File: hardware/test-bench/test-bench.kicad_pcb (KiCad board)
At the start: 2 copper layers, 90 x 90 mm, 35 parts, among them J1 Conn_Mem_Ext, J2 Conn_Reg, J3 SWD, J4 Conn_Mem, J5 FTDI, J6 Conn_Power, SW1 SW_Push_4pin, SW2 SW_Push_4pin, U1 STM32G030F6, U2 MCP23S17_SS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

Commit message: Added test points
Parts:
- added TP1: TestPoint, TestPoint:TestPoint_THTPad_D2.0mm_Drill1.0mm, F.Cu at (135.6, 51.6)
- added TP2: TestPoint, TestPoint:TestPoint_THTPad_D2.0mm_Drill1.0mm, F.Cu at (180.8, 46.8)
- added TP3: TestPoint, TestPoint:TestPoint_THTPad_D2.0mm_Drill1.0mm, F.Cu at (189.8, 75.6)
- added TP4: TestPoint, TestPoint:TestPoint_THTPad_D2.0mm_Drill1.0mm, F.Cu at (133.4, 91.4)
- added TP5: TestPoint, TestPoint:TestPoint_Pad_2.0x2.0mm, F.Cu at (189.8, 80.7)
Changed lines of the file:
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@@
     (tracks 1000)
     (zones 0)
-    (modules 35)
+    (modules 40)
     (nets 118)
   )
@@
     (mod_text_size 1 1)
     (mod_text_width 0.15)
-    (pad_size 1.75 0.45)
+    (pad_size 2 2)
     (pad_drill 0)
     (pad_to_mask_clearance 0.051)
@@
     )
   )
+  (module TestPoint:TestPoint_THTPad_D2.0mm_Drill1.0mm (layer F.Cu)
+    (at 135.6 51.6)
+    (descr "THT pad as test Point, diameter 2.0mm, hole diameter 1.0mm")
+    (tags "test point THT pad")
+    (attr virtual)
+    (fp_text reference TP1 (at 0 -1.998) (layer F.SilkS) hide
+      (effects (font (size 1 1) (thickness 0.15)))
+    )
+    (fp_text value TestPoint (at 0 2.05) (layer F.Fab)
+      (effects (font (size 1 1) (thickness 0.15)))
+    )
+    (fp_circle (center 0 0) (end 0 1.2) (layer F.SilkS) (width 0.12))
+    (fp_circle (center 0 0) (end 1.5 0) (layer F.CrtYd) (width 0.05))
+    (fp_text user %R (at 0 -2) (layer F.Fab)
+      (effects (font (size 1 1) (thickness 0.15)))
+    )
+    (pad 1 thru_hole circle (at 0 0) (size 2 2) (drill 1) (layers *.Cu *.Mask)
+      (net 8 GND))
+  )
+  (module TestPoint:TestPoint_THTPad_D2.0mm_Drill1.0mm (layer F.Cu)
+    (at 180.8 46.8)
+    (descr "THT pad as test Point, diameter 2.0mm, hole diameter 1.0mm")
+    (tags "test point THT pad")
+    (attr virtual)
+    (fp_text reference TP2 (at 0 -1.998) (layer F.SilkS) hide
+      (effects (font (size 1 1) (thickness 0.15)))
+    )
+    (fp_text value TestPoint (at 0 2.05) (layer F.Fab)
+      (effects (font (size 1 1) (thickness 0.15)))
+    )
+    (fp_text user %R (at 0 -2) (layer F.Fab)
+      (effects (font (size 1 1) (thickness 0.15)))
+    )
+    (fp_circle (center 0 0) (end 1.5 0) (layer F.CrtYd) (width 0.05))
+    (fp_circle (center 0 0) (end 0 1.2) (layer F.SilkS) (width 0.12))
+    (pad 1 thru_hole circle (at 0 0) (size 2 2) (drill 1) (layers *.Cu *.Mask)
+      (net 8 GND))
+  )
+  (module TestPoint:TestPoint_THTPad_D2.0mm_Drill1.0mm (layer F.Cu)
+    (at 189.8 75.6)
+    (descr "THT pad as test Point, diameter 2.0mm, hole diameter 1.0mm")
+    (tags "test point THT pad")
+    (attr virtual)
+    (fp_text reference TP3 (at 0 -1.998) (layer F.SilkS) hide
+      (effects (font (size 1 1) (thickness 0.15)))
+    )
+    (fp_text value TestPoint (at 0 2.05) (layer F.Fab)
+      (effects (font (size 1 1) (thickness 0.15)))
+    )
+    (fp_circle (center 0 0) (end 0 1.2) (layer F.SilkS) (width 0.12))
+    (fp_circle (center 0 0) (end 1.5 0) (layer F.CrtYd) (width 0.05))
+    (fp_text user %R (at 0 -2) (layer F.Fab)
+      (effects (font (size 1 1) (thickness 0.15)))
+    )
+    (pad 1 thru_hole circle (at 0 0) (size 2 2) (drill 1) (layers *.Cu *.Mask)
+      (net 8 GND))
+  )
+  (module TestPoint:TestPoint_THTPad_D2.0mm_Drill1.0mm (layer F.Cu)
+    (at 133.4 91.4)
+    (descr "THT pad as test Point, diameter 2.0mm, hole diameter 1.0mm")
+    (tags "test point THT pad")
+    (attr virtual)
+    (fp_text reference TP4 (at 0 -1.998) (layer F.SilkS) hide
+      (effects (font (size 1 1) (thickness 0.15)))
+    )
+    (fp_text value TestPoint (at 0 2.05) (layer F.Fab)
+      (effects (font (size 1 1) (thickness 0.15)))
+    )
+    (fp_text user %R (at 0 -2) (layer F.Fab)
+      (effects (font (size 1 1) (thickness 0.15)))
+    )
+    (fp_circle (center 0 0) (end 1.5 0) (layer F.CrtYd) (width 0.05))
+    (fp_circle (center 0 0) (end 0 1.2) (layer F.SilkS) (width 0.12))
+    (pad 1 thru_hole circle (at 0 0) (size 2 2) (drill 1) (layers *.Cu *.Mask)
+      (net 8 GND))
+  )
+  (module TestPoint:TestPoint_Pad_2.0x2.0mm (layer F.Cu)
+    (at 189.8 80.675)
+    (descr "SMD rectangular pad as test Point, square 2.0mm side length")
+    (tags "test point SMD pad rectangle square")
+    (attr virtual)
+    (fp_text reference TP5 (at 0 -1.998) (layer F.SilkS) hide
+      (effects (font (size 1 1) (thickness 0.15)))
+    )
+    (fp_text value TestPoint (at 0 2.05) (layer F.Fab)
+      (effects (font (size 1 1) (thickness 0.15)))
+    )
+    (fp_text user %R (at 0 -2) (layer F.Fab)
+      (effects (font (size 1 1) (thickness 0.15)))
+    )
+    (fp_line (start -1.2 -1.2) (end 1.2 -1.2) (layer F.SilkS) (width 0.12))
+    (fp_line (start 1.2 -1.2) (end 1.2 1.2) (layer F.SilkS) (width 0.12))
+    (fp_line (start 1.2 1.2) (end -1.2 1.2) (layer F.SilkS) (width 0.12))
+    (fp_line (start -1.2 1.2) (end -1.2 -1.2) (layer F.SilkS) (width 0.12))
+    (fp_line (start -1.5 -1.5) (end 1.5 -1.5) (layer F.CrtYd) (width 0.05))
+    (fp_line (start -1.5 -1.5) (end -1.5 1.5) (layer F.CrtYd) (width 0.05))
+    (fp_line (start 1.5 1.5) (end 1.5 -1.5) (layer F.CrtYd) (width 0.05))
+    (fp_line (start 1.5 1.5) (end -1.5 1.5) (layer F.CrtYd) (width 0.05))
+    (pad 1 smd rect (at 0 0) (size 2 2) (layers F.Cu F.Mask)
+      (net 7 VCC))
+  )
   (gr_text JLCJLCJLCJLC (at 162 27.2) (layer F.SilkS)

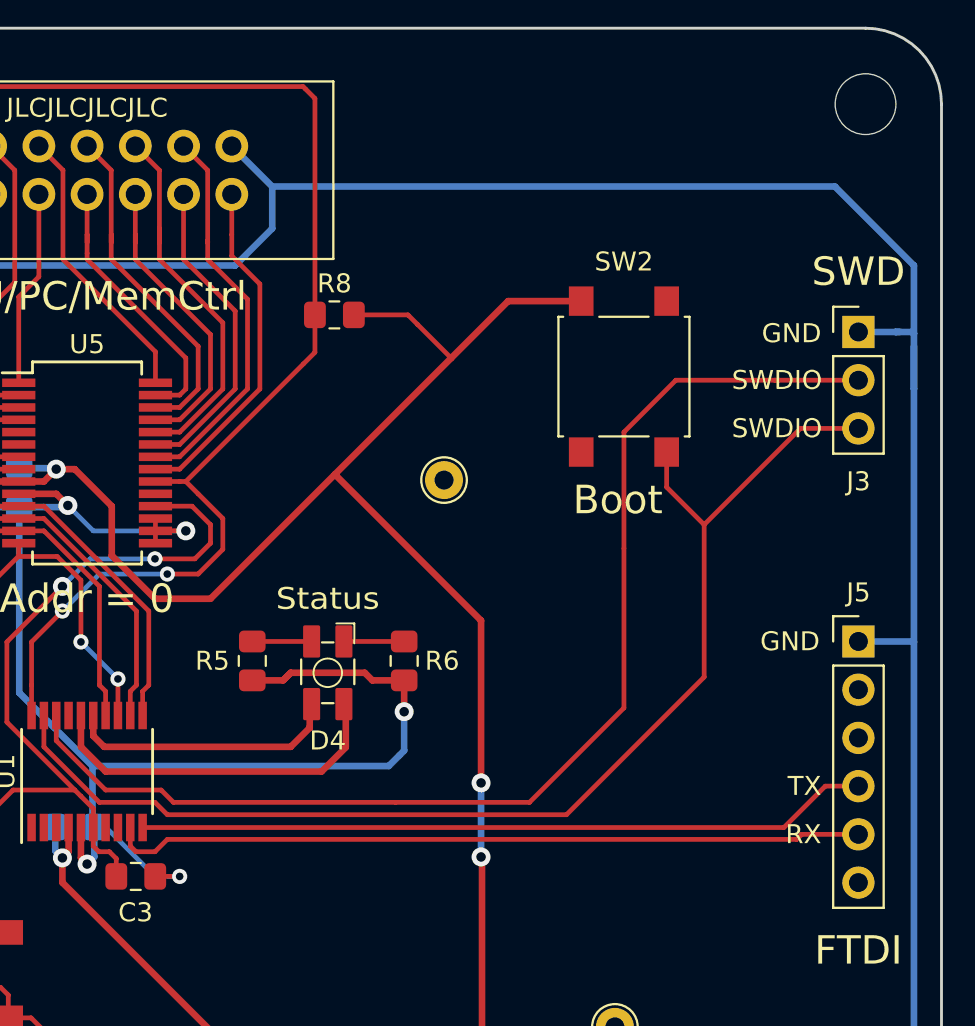
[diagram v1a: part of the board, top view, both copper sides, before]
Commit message: Add J-LINK 10-pin SWD header
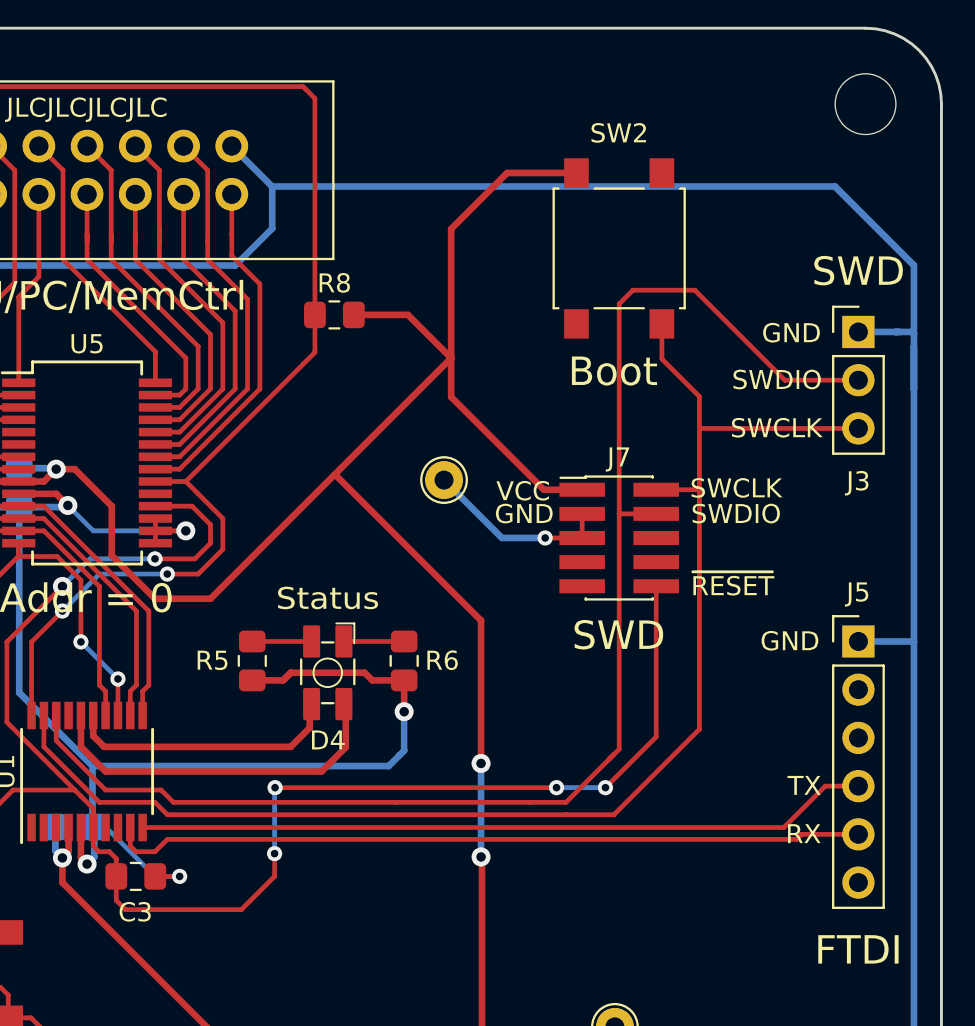
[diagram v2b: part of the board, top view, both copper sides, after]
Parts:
- added J7: J_LINK_SWD, Connector_PinHeader_1.27mm:PinHeader_2x05_P1.27mm_Vertical_SMD, F.Cu at (190.0, 49.9)
- moved SW2 6.75 mm to (190.0, 34.6)
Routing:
- net /~RESET: track 138.8 -> 183.1 mm, vias 10 -> 14
- net VCC: track 393.2 -> 410.7 mm
- net /SWDIO: track 62.8 -> 74.1 mm
- net GND: track 469.9 -> 479.7 mm, vias 15 -> 16
- net /SWCLK: track 63.8 -> 72.4 mm
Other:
- board text added: "SWCLK"
- board text added: "VCC"
- board text added: "~RESET"

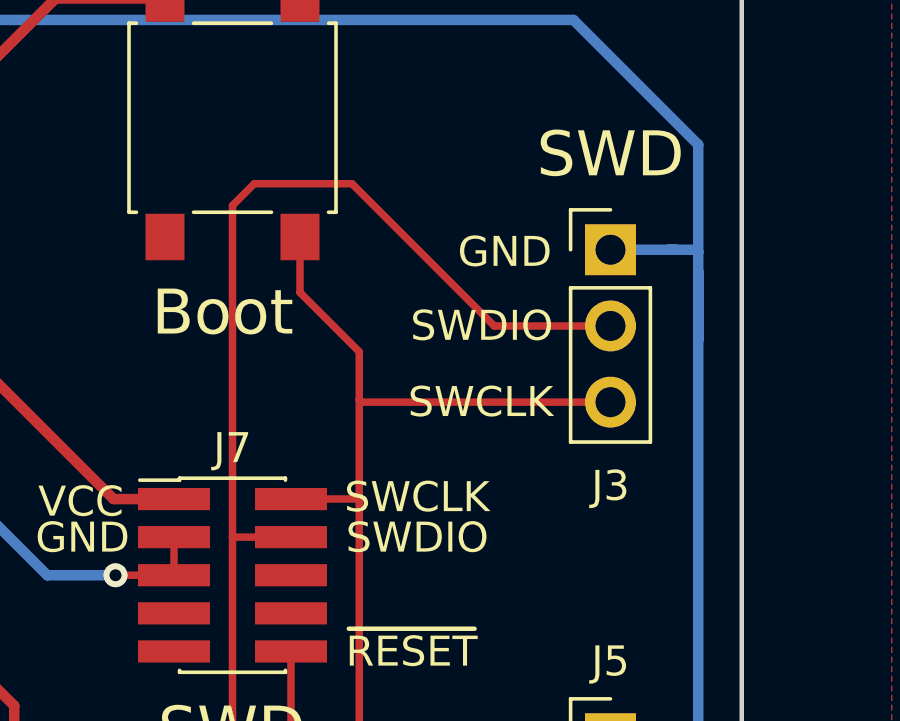
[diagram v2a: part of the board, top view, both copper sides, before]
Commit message: Fix SWD pinout
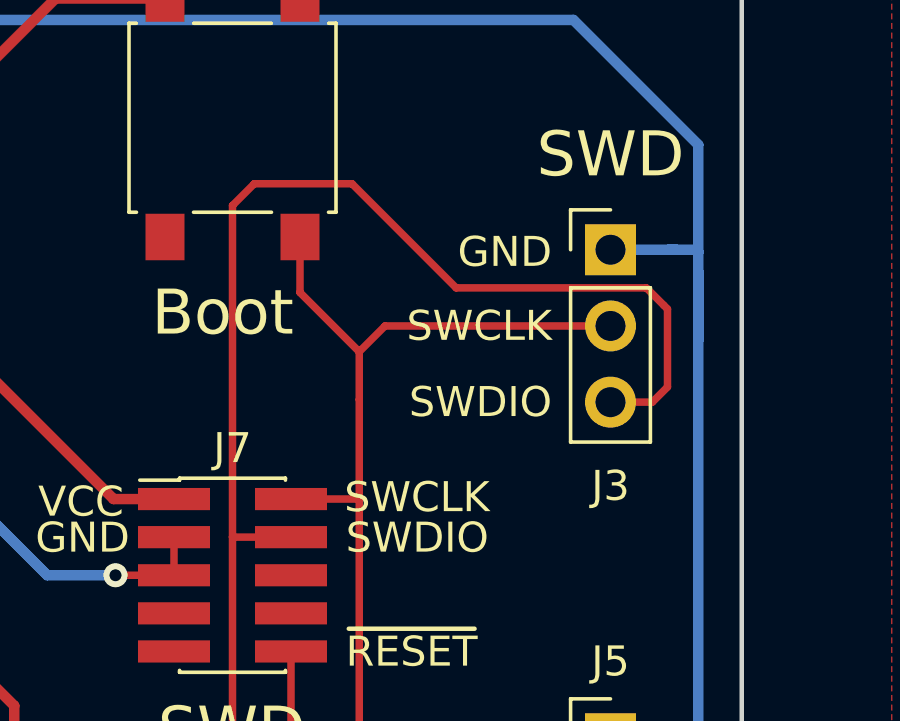
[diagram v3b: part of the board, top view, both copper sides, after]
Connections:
- J3 pad 2: /SWDIO -> /SWCLK
- J3 pad 3: /SWCLK -> /SWDIO
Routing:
- net /SWDIO: track 74.1 -> 80.5 mm
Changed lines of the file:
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@@
     (thickness 1.6)
     (drawings 42)
-    (tracks 1033)
+    (tracks 1038)
     (zones 0)
     (modules 41)
@@
   )
   (setup
-    (last_trace_width 0.35)
+    (last_trace_width 0.25)
     (user_trace_width 0.35)
     (user_trace_width 0.5)
@@
       (net 8 GND))
     (pad 2 thru_hole oval (at 0 2.54) (size 1.7 1.7) (drill 1) (layers *.Cu *.Mask)
+      (net 10 /SWCLK))
+    (pad 3 thru_hole oval (at 0 5.08) (size 1.7 1.7) (drill 1) (layers *.Cu *.Mask)
       (net 9 /SWDIO))
-    (pad 3 thru_hole oval (at 0 5.08) (size 1.7 1.7) (drill 1) (layers *.Cu *.Mask)
-      (net 10 /SWCLK))
     (model ${KISYS3DMOD}/Connector_PinHeader_2.54mm.3dshapes/PinHeader_1x03_P2.54mm_Vertical.wrl
       (at (xyz 0 0 0))
@@
     (effects (font (size 1.5 1.5) (thickness 0.3)))
   )
-  (gr_text SWCLK (at 200.72 44.08) (layer F.SilkS)
+  (gr_text SWCLK (at 200.675 41.54) (layer F.SilkS)
     (effects (font (size 1 1) (thickness 0.15)) (justify right))
   )
-  (gr_text SWDIO (at 200.72 41.54) (layer F.SilkS)
+  (gr_text SWDIO (at 200.675 44.08) (layer F.SilkS)
     (effects (font (size 1 1) (thickness 0.15)) (justify right))
   )
@@
   (segment (start 190.03 48.58) (end 190.025 48.575) (width 0.25) (layer F.Cu) (net 9))
   (segment (start 191.975 48.58) (end 190.03 48.58) (width 0.25) (layer F.Cu) (net 9))
-  (segment (start 190.025 37.525) (end 190.025 48.575) (width 0.25) (layer F.Cu) (net 9))
   (segment (start 190.025 48.575) (end 190.025 60.975) (width 0.25) (layer F.Cu) (net 9))
   (segment (start 187.225 63.775) (end 189.5 61.5) (width 0.25) (layer F.Cu) (net 9))
   (segment (start 190.025 60.975) (end 189.5 61.5) (width 0.25) (layer F.Cu) (net 9))
   (segment (start 189.5 61.5) (end 189.75 61.25) (width 0.25) (layer F.Cu) (net 9))
-  (segment (start 194.01 36.8) (end 198.75 41.54) (width 0.25) (layer F.Cu) (net 9))
+  (segment (start 204.525 40.975) (end 204.525 43.575) (width 0.25) (layer F.Cu) (net 9))
+  (segment (start 204.02 44.08) (end 202.625 44.08) (width 0.25) (layer F.Cu) (net 9))
+  (segment (start 204.525 43.575) (end 204.02 44.08) (width 0.25) (layer F.Cu) (net 9))
+  (segment (start 203.82 40.27) (end 204.403 40.853) (width 0.25) (layer F.Cu) (net 9))
+  (segment (start 204.403 40.853) (end 204.525 40.975) (width 0.25) (layer F.Cu) (net 9))
   (segment (start 190.75 36.8) (end 194.01 36.8) (width 0.25) (layer F.Cu) (net 9))
-  (segment (start 198.75 41.54) (end 202.625 41.54) (width 0.25) (layer F.Cu) (net 9))
-  (segment (start 190.75 36.8) (end 190.025 37.525) (width 0.25) (layer F.Cu) (net 9))
+  (segment (start 197.48 40.27) (end 203.82 40.27) (width 0.25) (layer F.Cu) (net 9))
+  (segment (start 190.025 48.575) (end 190.025 37.525) (width 0.25) (layer F.Cu) (net 9))
+  (segment (start 190.025 37.525) (end 190.75 36.8) (width 0.25) (layer F.Cu) (net 9))
+  (segment (start 194.01 36.8) (end 197.48 40.27) (width 0.25) (layer F.Cu) (net 9))
   (segment (start 192.275 40.425) (end 194.25 42.4) (width 0.25) (layer F.Cu) (net 10))
   (segment (start 192.275 38.575) (end 192.275 40.425) (width 0.25) (layer F.Cu) (net 10))
@@
   (segment (start 194.25 59.925) (end 189.75 64.425) (width 0.25) (layer F.Cu) (net 10))
   (segment (start 187.25 64.425) (end 189.75 64.425) (width 0.25) (layer F.Cu) (net 10))
-  (segment (start 194.33 44.08) (end 194.25 44) (width 0.25) (layer F.Cu) (net 10))
-  (segment (start 202.625 44.08) (end 194.33 44.08) (width 0.25) (layer F.Cu) (net 10))
   (segment (start 194.25 42.4) (end 194.25 44) (width 0.25) (layer F.Cu) (net 10))
   (segment (start 194.25 44) (end 194.25 47.3) (width 0.25) (layer F.Cu) (net 10))
+  (segment (start 195.11 41.54) (end 194.25 42.4) (width 0.25) (layer F.Cu) (net 10))
+  (segment (start 202.625 41.54) (end 195.11 41.54) (width 0.25) (layer F.Cu) (net 10))
   (segment (start 153.55 57.6) (end 142.175 68.975) (width 0.25) (layer F.Cu) (net 14))
   (segment (start 142.175 68.975) (end 142.175 71.6) (width 0.25) (layer F.Cu) (net 14))
